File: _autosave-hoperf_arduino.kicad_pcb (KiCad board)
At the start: 2 copper layers, 35 parts, among them Q1 DMN6140L, Q2 DMN6140L, Q3 DMN6140L, Q4 DMN6140L, Q5 DMN6140L, Q6 DMN6140L, Q7 DMN6140L, SW1 SW_SPST, U1 AZ1117-3.3, U2 RFM95W-915S2

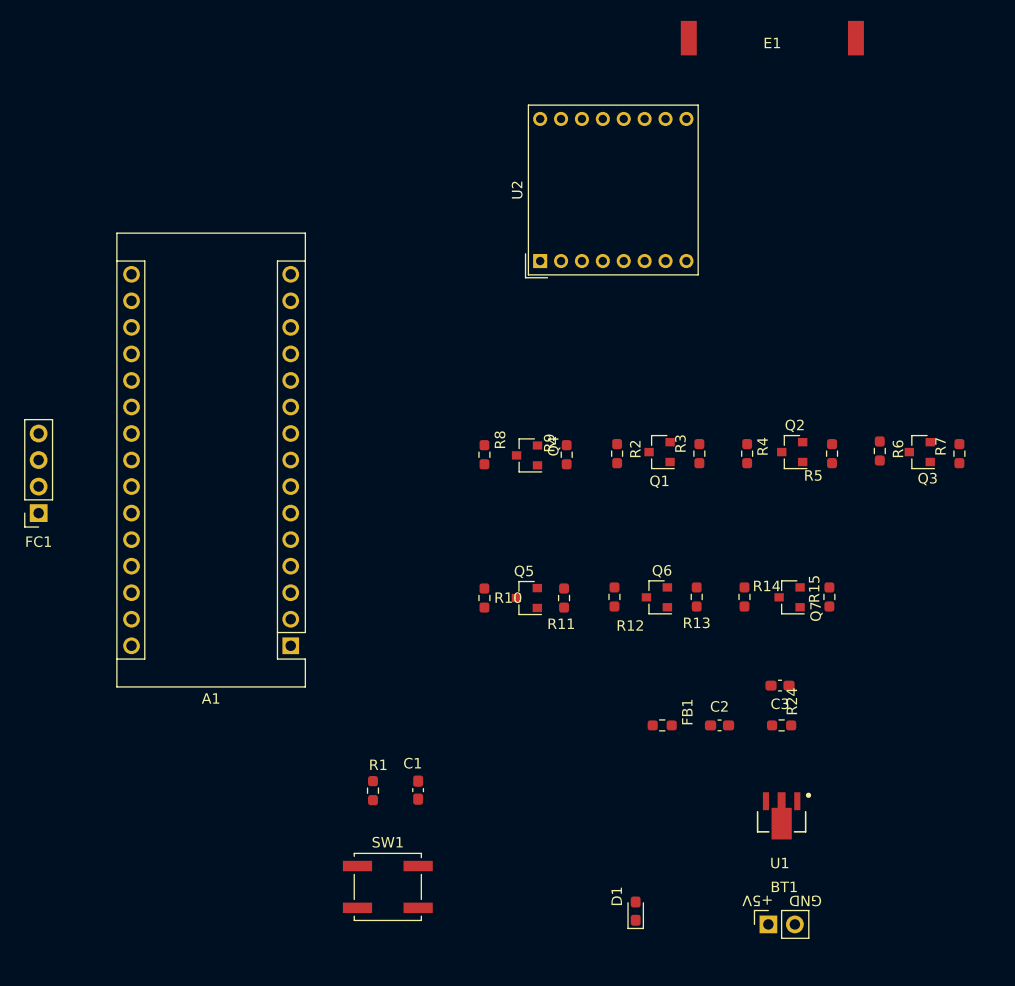
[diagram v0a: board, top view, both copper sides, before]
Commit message: remove unncessary parts, update sch
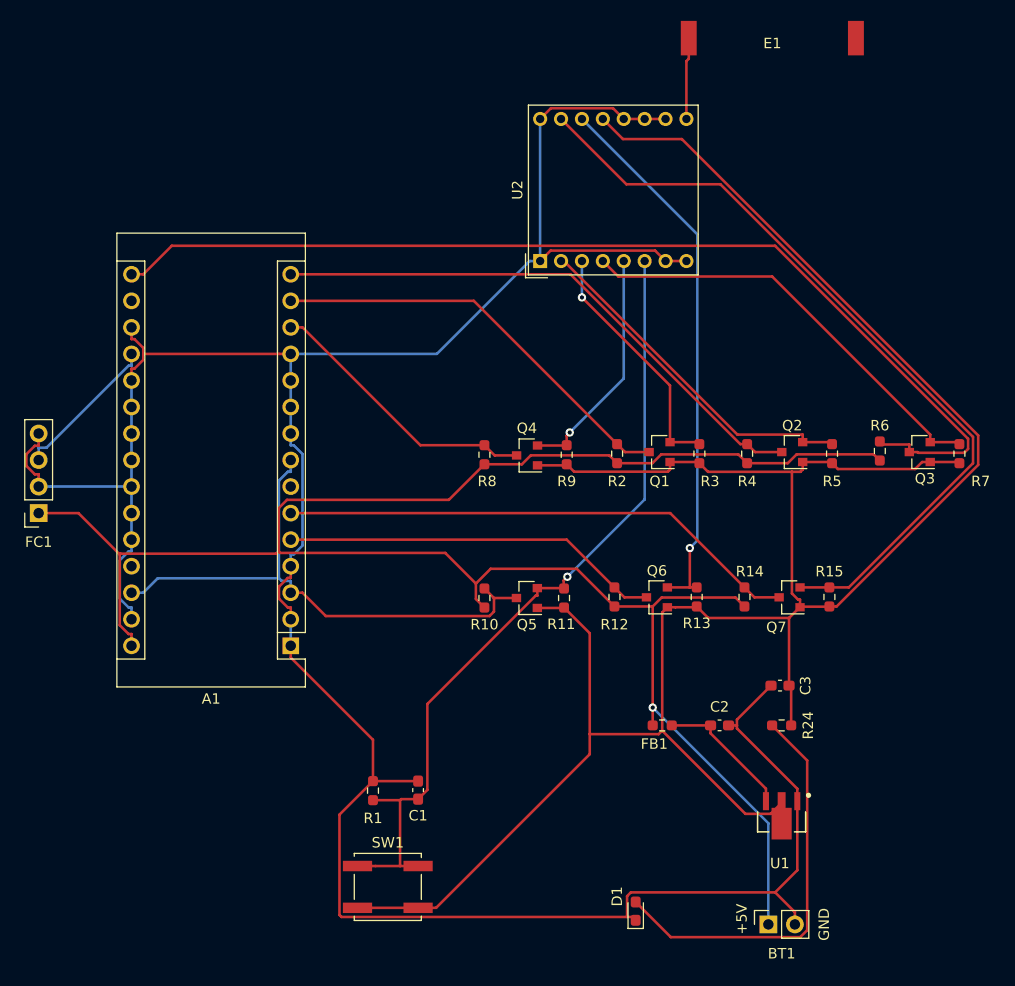
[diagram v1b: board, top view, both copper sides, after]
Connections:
- A1 pad 1: (no net) -> GND
- A1 pad 10: (no net) -> GND
- A1 pad 11: (no net) -> GND
- A1 pad 12: (no net) -> GND
- A1 pad 18: (no net) -> GND
- A1 pad 2: (no net) -> GND
- A1 pad 20: (no net) -> GND
- A1 pad 21: (no net) -> GND
- A1 pad 22: (no net) -> GND
- A1 pad 23: (no net) -> GND
- A1 pad 24: (no net) -> GND
- A1 pad 25: (no net) -> GND
- A1 pad 26: (no net) -> GND
- A1 pad 3: (no net) -> /H_RESET
- A1 pad 9: (no net) -> GND
- U2 pad 11: (no net) -> GND
- U2 pad 12: (no net) -> GND
- U2 pad 16: (no net) -> GND
- U2 pad 7: (no net) -> GND
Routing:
- net GND: track 0.00 -> 267.9 mm
- net +3V3: track 0.00 -> 235.2 mm
- net +5V: track 0.00 -> 187.5 mm, vias 0 -> 1
- net /H_SCK: track 0.00 -> 99.3 mm
- net /L_RESET: track 0.00 -> 78.6 mm, vias 0 -> 1
- net /L_DIO1: track 0.00 -> 76.0 mm
- net /H_RESET: track 0.00 -> 54.3 mm
- net /H_MISO: track 0.00 -> 54.1 mm
- net /L_DIO0: track 0.00 -> 52.5 mm, vias 0 -> 1
- net /H_DIO1: track 0.00 -> 50.1 mm
- net /L_SCK: track 0.00 -> 41.8 mm
- net /H_MOSI: track 0.00 -> 40.3 mm
- net Net-(D1-Pad2): track 0.00 -> 39.1 mm
- net /H_DIO0: track 0.00 -> 36.3 mm
- net /L_MISO: track 0.00 -> 33.6 mm
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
